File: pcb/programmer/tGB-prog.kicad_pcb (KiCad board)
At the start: 2 copper layers, 25.2 x 31 mm, 34 parts, among them J1 ZX62-B-5PA(33), J2 PROG_PORT, U1 FT2232D, U2 93LC56BT-I/OT, U3 TPS79901DDCR, Y1 ML49G 6MHz

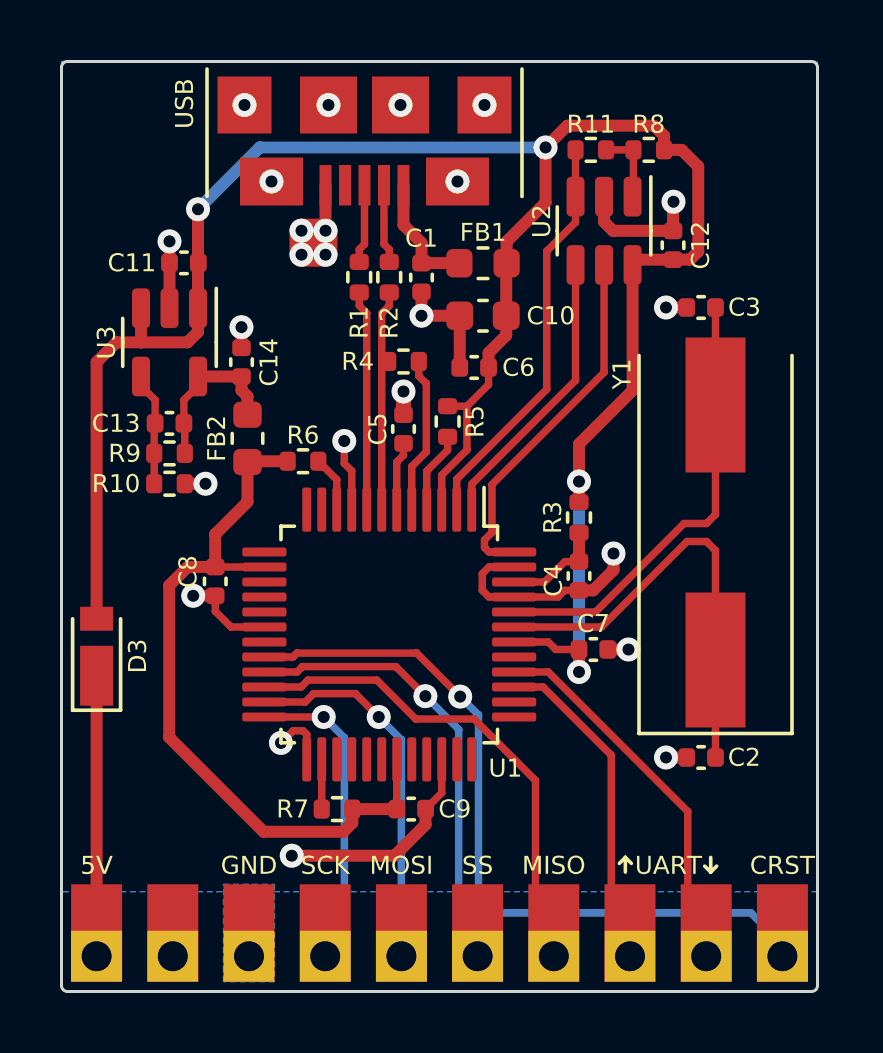
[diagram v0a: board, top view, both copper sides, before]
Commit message: fix D+ and D- polarity reversal on USB
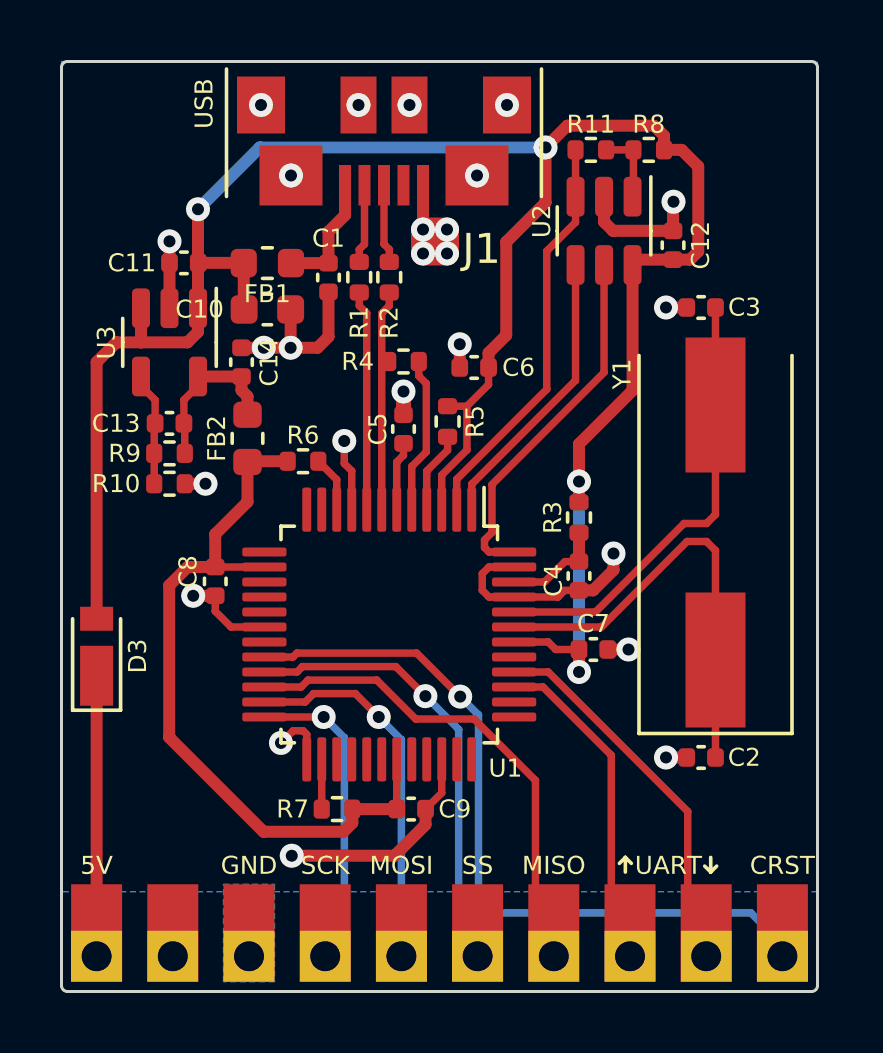
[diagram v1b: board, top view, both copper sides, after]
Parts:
- J1: value ZX62-B-5PA(33) -> ZX62R-B-5P; footprint ZX62-B-5PA:ZX62-B-5PA(33) -> ZX62R-B-5P:ZX62R-B-5P
- moved C10 7.19 mm to (66.9, 77.3), turned to 0 degrees
- moved FB1 7.19 mm to (66.9, 75.7), turned to 180 degrees
- moved C1 3.10 mm to (68.9, 76.2)
- moved J1 0.65 mm to (70.8, 69.0)
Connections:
- J1 pad 2: Net-(J1-Pad2) -> /USB_D-
- J1 pad 3: Net-(J1-Pad3) -> /USB_D+
- R1 pad 1: Net-(J1-Pad3) -> /USB_D-
- R2 pad 2: Net-(J1-Pad2) -> /USB_D+
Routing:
- net +5V: track 73.6 -> 76.7 mm
- net Net-(J1-Pad3): track 2.63 -> 0.00 mm
- net Net-(J1-Pad2): track 2.63 -> 0.00 mm
- net /USB_D-: track 0.00 -> 2.63 mm
- net /USB_D+: track 0.00 -> 2.63 mm
- net GND: track 41.0 -> 43.1 mm, vias 24 -> 25

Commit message: change Y1 parts, centering of USB connector
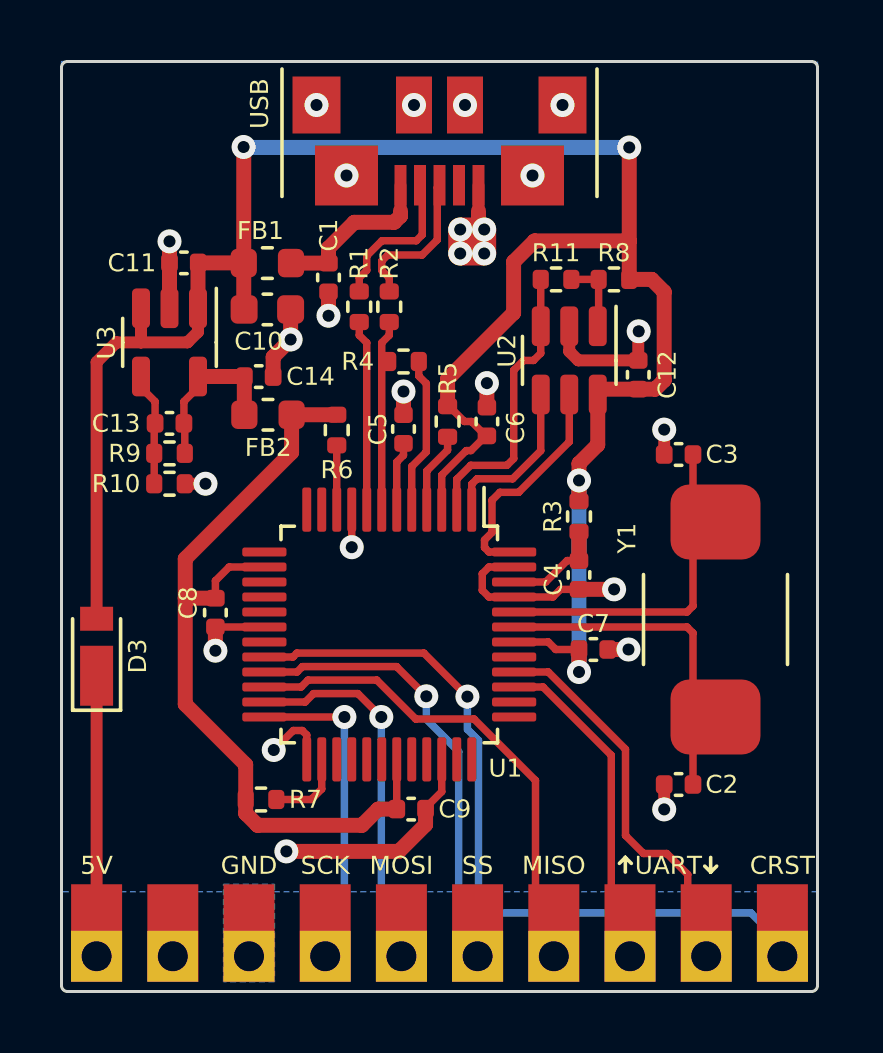
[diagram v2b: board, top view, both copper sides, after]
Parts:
- Y1: value ML49G 6MHz -> NX8045GB-6MHZ-STD-CSF-3; footprint Crystal:Crystal_SMD_HC49-SD -> Crystal:Crystal_SMD_TXC_AX_8045-2Pin_8.0x4.5mm
- moved C3 4.96 mm to (80.6, 82.1)
- moved R11 4.47 mm to (76.5, 76.3)
- moved R8 4.47 mm to (78.4, 76.3)
- moved U2 4.47 mm to (76.9, 79.0)
- moved C12 4.47 mm to (79.2, 79.4)
- moved Y1 2.90 mm to (81.8, 87.6)
- moved R7 2.56 mm to (66.7, 93.6), turned to 180 degrees
- moved J1 1.85 mm to (72.6, 69.0)
- moved C6 1.85 mm to (74.2, 81.0), turned to 90 degrees
- moved R6 1.53 mm to (69.2, 81.3), turned to 90 degrees
- moved C2 1.17 mm to (80.6, 93.1)
- moved FB2 1.04 mm to (66.9, 80.8), turned to 0 degrees
- moved C8 1.04 mm to (65.1, 87.4)
- moved R1 0.98 mm to (69.9, 77.2)
- moved R2 0.98 mm to (70.9, 77.2)
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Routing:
- net /EECS: track 12.1 -> 7.69 mm
- net GND: track 43.1 -> 38.7 mm
- net /EECLK: track 9.59 -> 5.49 mm
- net /EEDATA: track 13.6 -> 9.74 mm
- net Net-(C3-Pad1): track 15.0 -> 11.7 mm
- net Net-(C2-Pad1): track 14.9 -> 11.7 mm
- net +3V3: track 24.9 -> 27.6 mm
- net /USB_D-: track 2.63 -> 5.10 mm
- net /USB_D+: track 2.63 -> 5.10 mm
- net +5V: track 76.7 -> 74.7 mm
- net /VBUS: track 4.07 -> 5.62 mm
- net Net-(R7-Pad1): track 1.66 -> 2.65 mm
- net /USB_DP: track 7.56 -> 6.57 mm
- net /USB_DM: track 7.34 -> 6.36 mm

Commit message: add junpers for VDDIO supply from main board, add power LED
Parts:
- removed D3: RSX101VAM-30TR, Diode_SMD:D_TUMD2
- added C15: DNP, Capacitor_SMD:C_0603_1608Metric, F.Cu at (64.7, 92.8)
- added D1: SML-E12V8WT86, LED_Addition:LED_0603_1608Metric_Castellated, F.Cu at (82.5, 72.4)
- added D2: RSX101VAM-30TR, Diode_SMD:D_TUMD2, F.Cu at (61.2, 88.8)
- added R12: DNP, Resistor_SMD:R_0603_1608Metric, F.Cu at (63.1, 92.8)
- added R13: 4.7kΩ, Resistor_SMD:R_0402_1005Metric, F.Cu at (80.5, 71.9)
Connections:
- J2 pad 2: unconnected-(J2-Pad2) -> /+3V3_GB
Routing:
- net /+3V3_GB: track 0.00 -> 4.66 mm
- net GND: track 38.7 -> 40.9 mm, vias 25 -> 27
- net +3V3: track 27.6 -> 29.8 mm
- net Net-(D1-Pad2): track 0.00 -> 1.66 mm
- net +5V: track 74.7 -> 75.7 mm
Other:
- board text added: "3.3V"

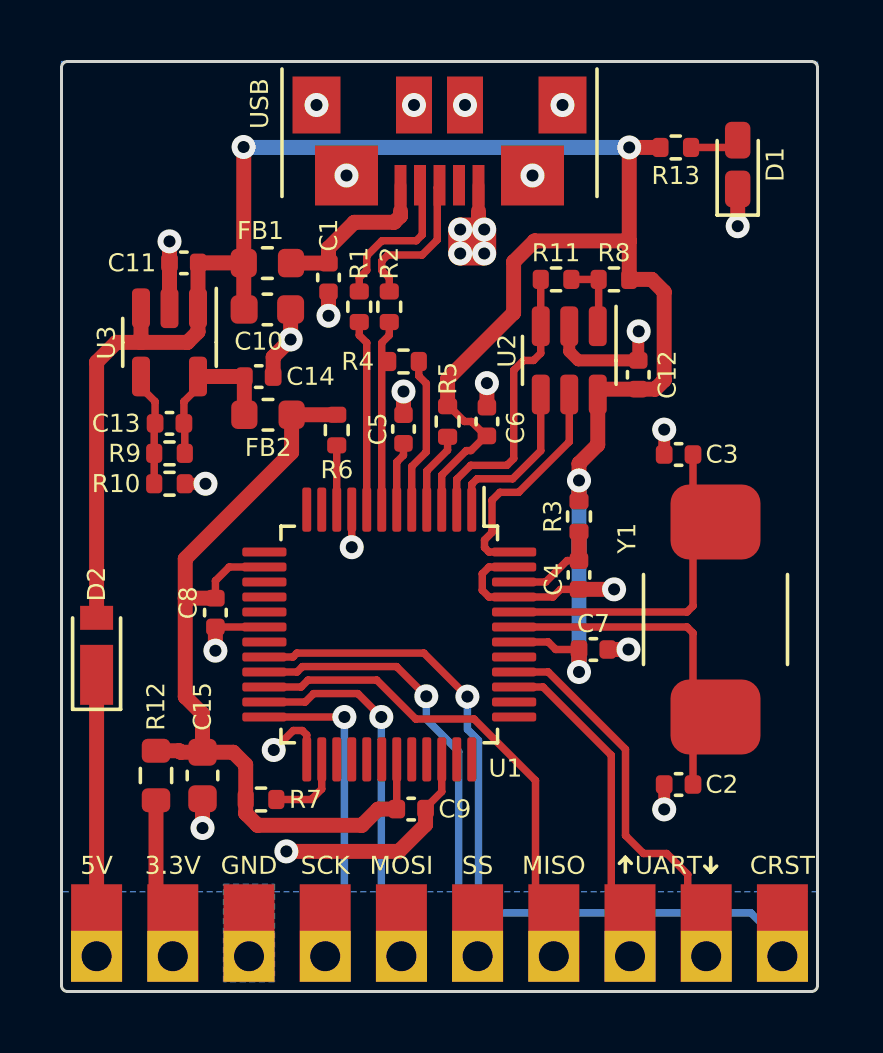
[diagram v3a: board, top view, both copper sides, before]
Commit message: separate USB GND and shield
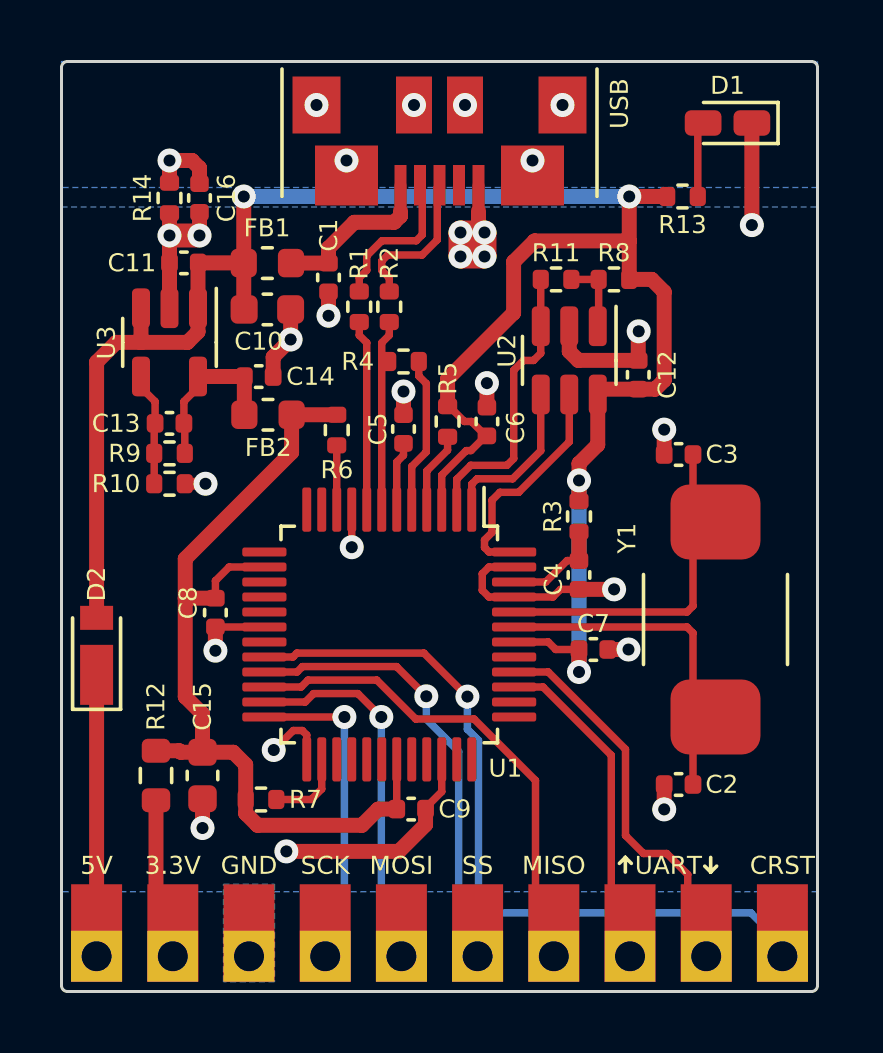
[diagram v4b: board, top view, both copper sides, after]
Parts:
- added C16: 10nF, Capacitor_SMD:C_0402_1005Metric, F.Cu at (64.6, 73.5)
- added R14: DNP, Resistor_SMD:R_0402_1005Metric, F.Cu at (63.6, 73.5)
- moved R13 1.65 mm to (80.7, 73.5)
- moved D1 1.43 mm to (82.2, 71.0), turned to 180 degrees
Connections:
- J1 pad 6: GND -> /SHIELD
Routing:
- net GND: track 40.9 -> 45.9 mm, vias 27 -> 22
- net +5V: track 75.7 -> 72.6 mm
- net /SHIELD: track 0.00 -> 2.36 mm, vias 0 -> 7
- net Net-(D1-Pad2): track 1.66 -> 2.52 mm
- added copper zone on B.Cu, net /SHIELD
